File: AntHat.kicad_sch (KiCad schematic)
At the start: 61 parts, among them J1 Raspberry_Pi_2_3, J10 0353180420, J11 0353180420, J2 0455580003, J3 PSU Comm, J4 61900411021, J5 61900411021, J6 61900411021, J7 61900411021, J8 0353180420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

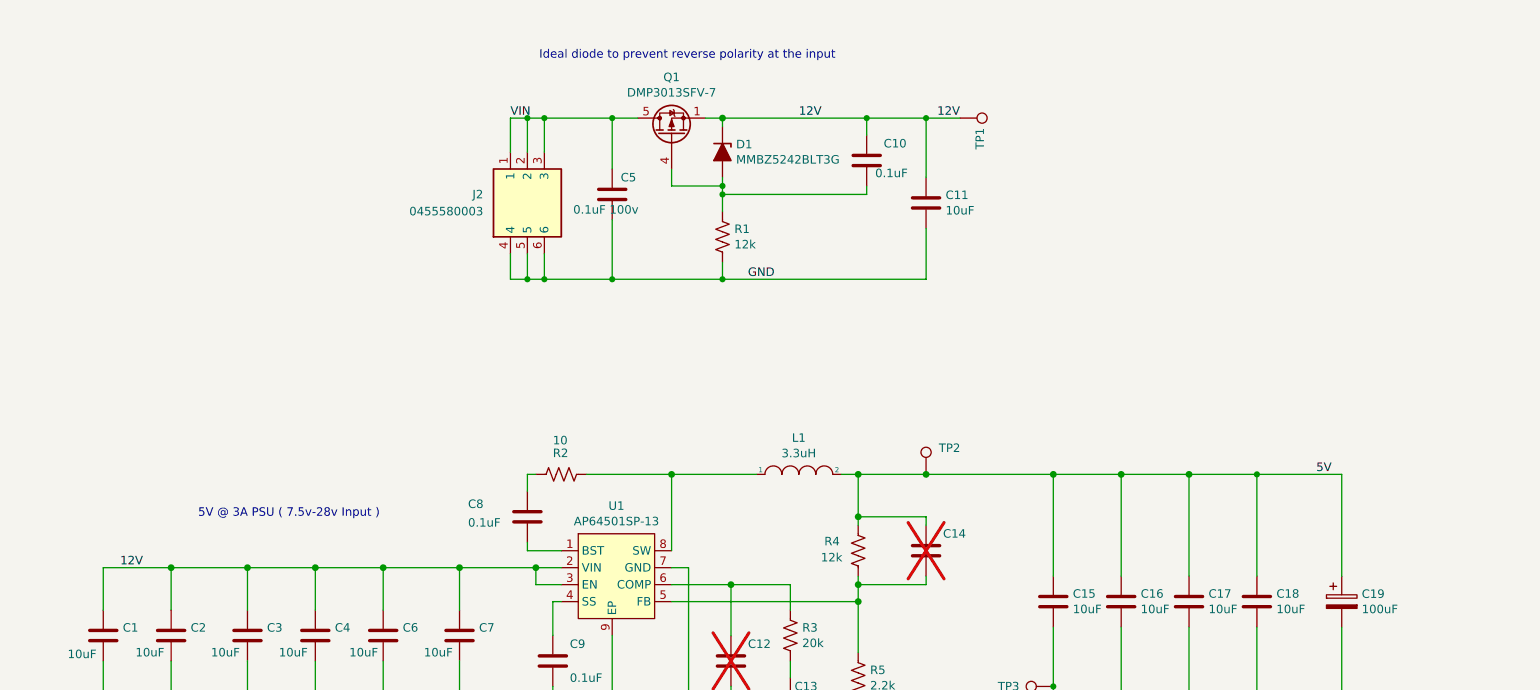
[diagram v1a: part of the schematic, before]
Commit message: started to add TPS259241
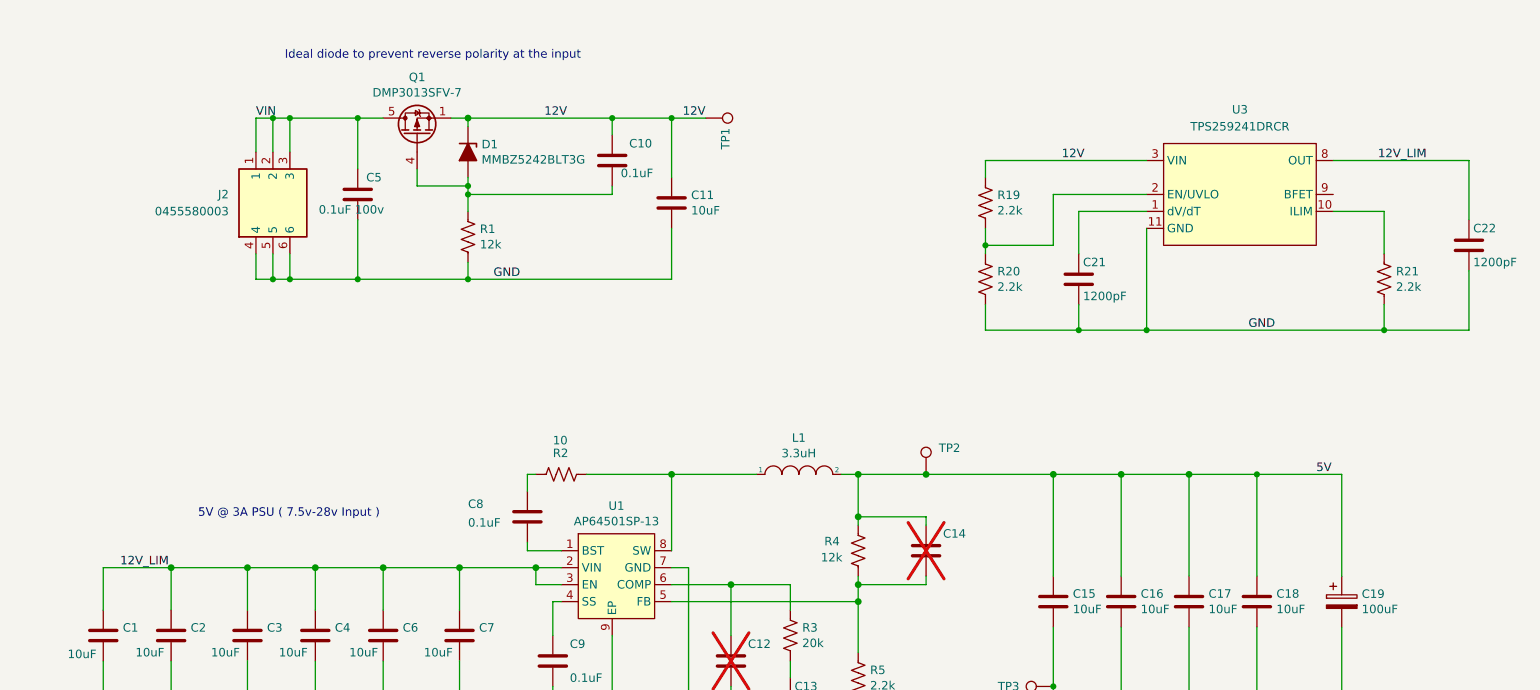
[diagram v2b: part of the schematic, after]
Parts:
- added C21, C22: 1200pF, Capacitor_SMD:C_0402_1005Metric, symbol Device:C
- added R19, R20, R21: 2.2k, Resistor_SMD:R_0402_1005Metric, symbol Device:R_US
- added U3: TPS259241DRCR, AntHat:VSON-10_L3.0-W3.0-P0.50-TL-EP, symbol AntHat:TPS259241DRCR
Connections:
- net 12V: now also R19.1, U3.3 (VIN), U3.4 (VIN), U3.5 (VIN); no longer C1.1, C2.1, C3.1, C4.1, C6.1, C7.1, U1.2 (VIN), U1.3 (EN)
- net GND: now also C21.2, C22.2, R20.2, R21.2, U3.11 (GND)
- new net: R19.2, R20.1, U3.2 (EN/UVLO)
- new net: C21.1, U3.1 (dV/dT)
- new net: R21.1, U3.10 (ILIM)
- new net 12V_LIM: C1.1, C2.1, C22.1, C3.1, C4.1, C6.1, C7.1, U1.2 (VIN), U1.3 (EN), U3.6 (OUT), U3.7 (OUT), U3.8 (OUT)
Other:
- moved on the sheet: C10, C11, C5, D1, J2, Q1, R1, TP1

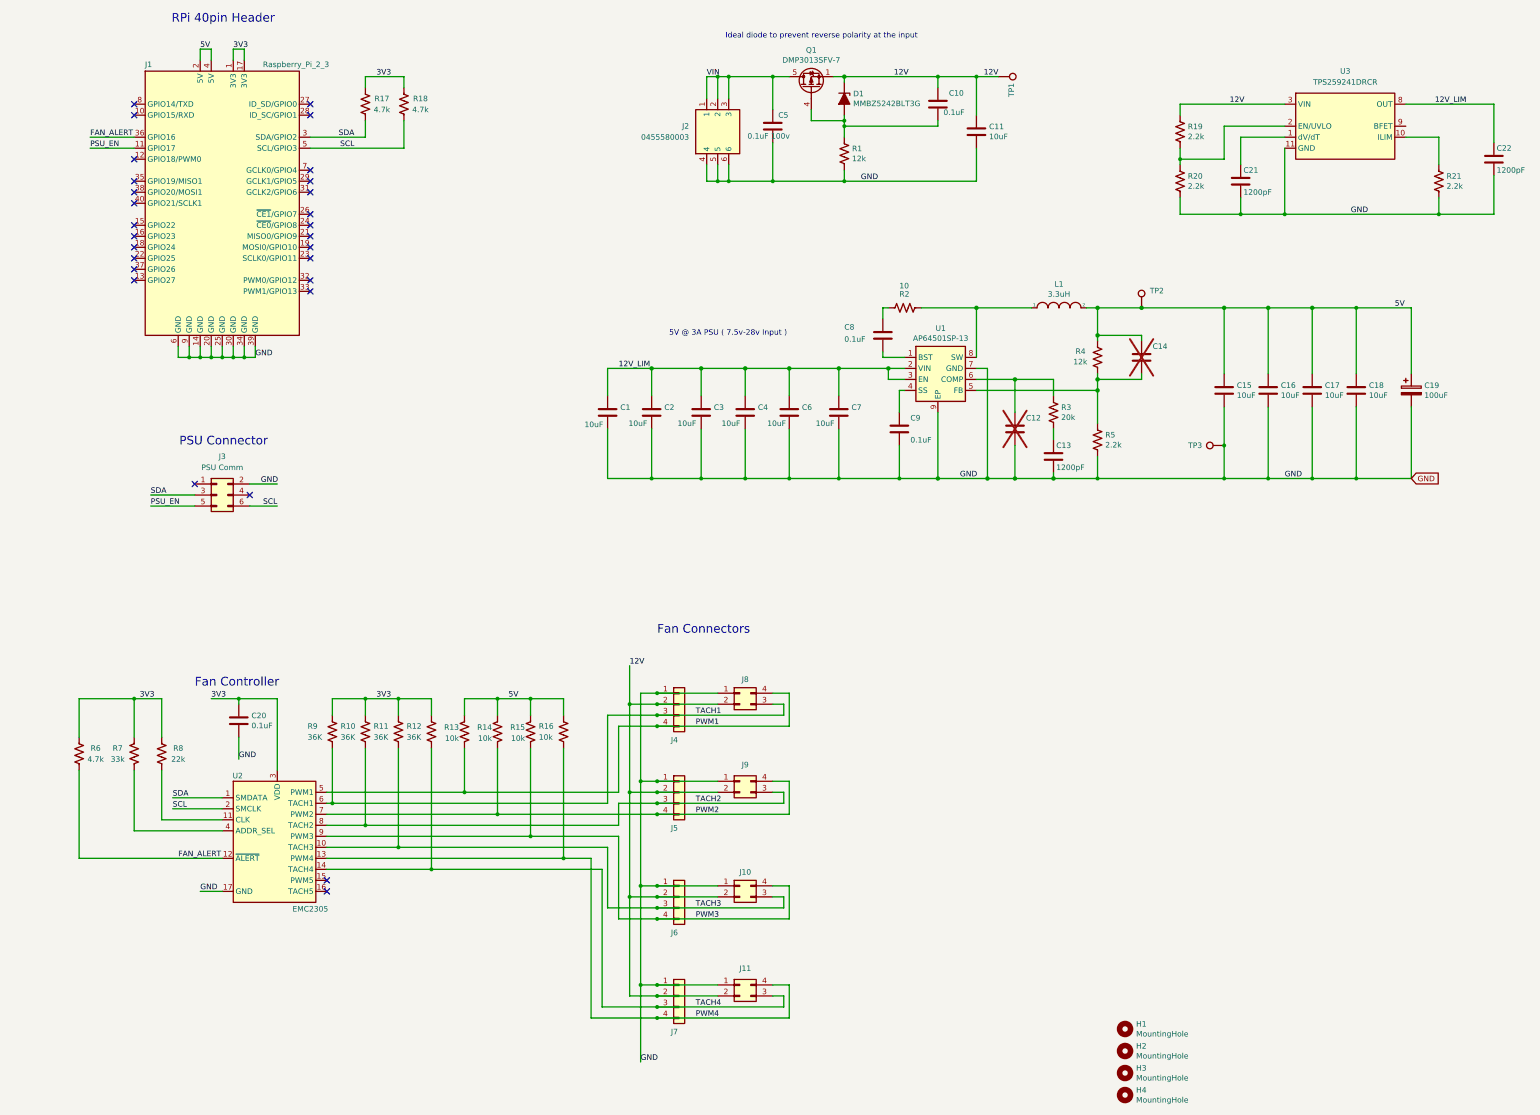
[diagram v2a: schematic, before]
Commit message: combined the fan connector styles. added some LCSC part numbers. switched PSU I2C over to GPIO for bit banging.
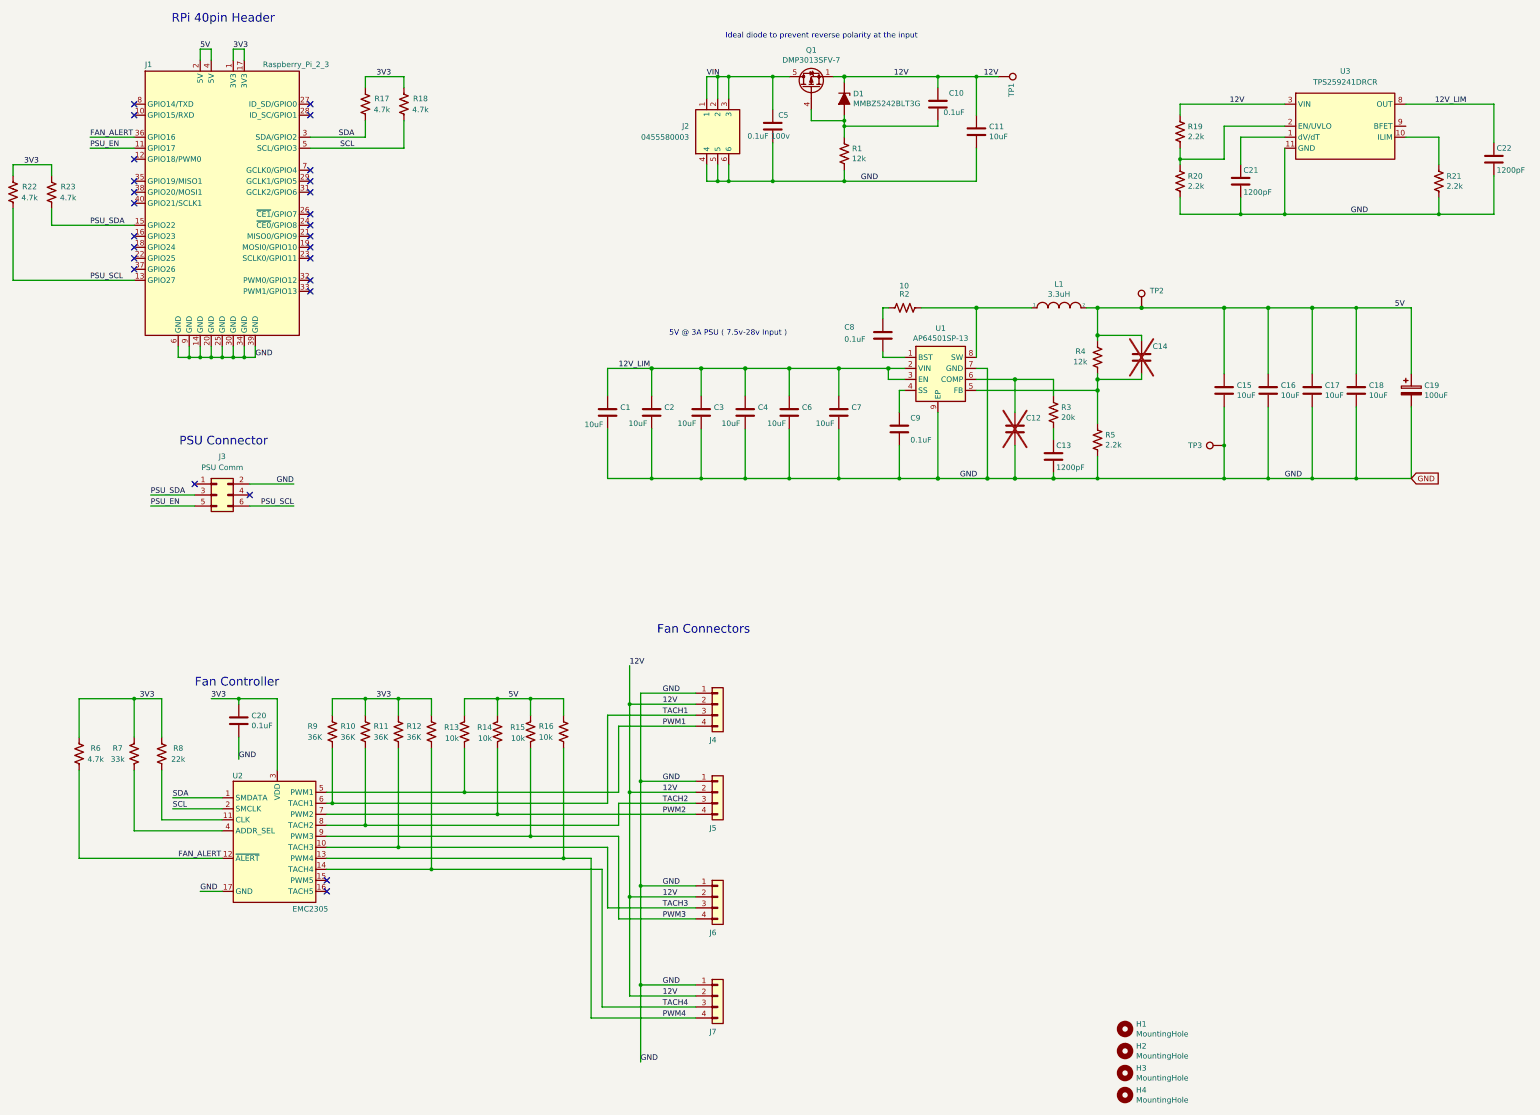
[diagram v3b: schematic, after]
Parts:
- removed J10, J11, J8, J9: 0353180420, AntHat:MOLEX_353180420, symbol Connector_Generic:Conn_02x02_Counter_Clockwise
- added R22, R23: 4.7k, Resistor_SMD:R_0402_1005Metric, symbol Device:R_US
- D1: LCSC (none) -> C12773; PARTNO MMBZ5242BLT3G -> LBZX84C12LT1G
- H1, H2, H3, H4: now left out of the parts list
- J1: LCSC (none) -> C2977589; LCSC Part C2977589 -> (none)
- J2: LCSC (none) -> C19188571; LCSC Part C19188571 -> (none)
- J3: LCSC (none) -> C2845614; LCSC Part C2845614 -> (none)
- J4, J5: footprint AntHat:CONN_61900411021_WRE -> AntHat:MOLEX_1x4_2x2_combo; LCSC (none) -> C2982043
- J6, J7: value 61900411021 -> 0353180420; footprint AntHat:CONN_61900411021_WRE -> AntHat:MOLEX_1x4_2x2_combo; DK 732-2701-ND -> WM13195-ND; LCSC (none) -> C54909; PARTNO 61900411021 -> 0353180420
- L1: LCSC (none) -> C189931; LCSC Part C189931 -> (none)
- Q1: LCSC (none) -> C264098; LCSC Part C264098 -> (none)
- U1: LCSC (none) -> C2071517
- U3: LCSC (none) -> C165131; LCSC Part C165131 -> (none)
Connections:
- net 3V3: now also R22.2, R23.2
- net SCL: no longer J3.6 (Pin_6)
- net SDA: no longer J3.3 (Pin_3)
- net PSU_SCL: now reaches J1.13 (GPIO27)
- net PSU_SCL: now also J3.6 (Pin_6), R22.1
- net PSU_SDA: now reaches J1.15 (GPIO22)
- net PSU_SDA: now also J3.3 (Pin_3), R23.1
- no-connect marks 28 -> 26
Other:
- moved on the sheet: J4, J5, J6, J7

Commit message: fixed the footprint & paste on the TPS259241 footprint. Generated and checked gerbers. Generated BOM. Generated iBOM
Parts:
- U3: DK (none) -> 296-44843-1-ND; PARTNO (none) -> TPS259241DRCR
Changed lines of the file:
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@@
 			)
 		)
-		(property "Datasheet" ""
+		(property "Datasheet" "https://www.ti.com/lit/ds/symlink/tps25924.pdf"
 			(at 330.2 58.42 0)
 			(effects
@@
 			(at 330.2 50.8 0)
 			(effects
+				(font
+					(size 1.27 1.27)
+				)
+				(hide yes)
+			)
+		)
+		(property "DK" "296-44843-1-ND"
+			(at 330.2 50.8 0)
+			(effects
+				(font
+					(size 1.27 1.27)
+				)
+				(hide yes)
+			)
+		)
+		(property "PARTNO" "TPS259241DRCR"
+			(at 330.2 50.8 0)
+			(effects

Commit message: added JLCPCB Parts to BOM. changed one CAP to bigger size, cleaned up layout. regenerated gerbers, BOM and CPOS
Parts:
- C1, C11, C15, C16, C17, C18, C2, C3, C4, C6, C7: LCSC (none) -> C15850; Voltage (none) -> 25V
- C10, C20, C8, C9: LCSC (none) -> C52923; Voltage (none) -> 25V
- C13, C21, C22: LCSC (none) -> C16529; Voltage (none) -> 25V
- C19: LCSC (none) -> C7222; Voltage (none) -> 10V
- C5: value 0.1uF 100v -> 0.1uF; footprint Capacitor_SMD:C_0402_1005Metric -> Capacitor_SMD:C_0805_2012Metric; DK 490-10458-1-ND -> (none); LCSC (none) -> C28233; PARTNO GRM155R62A104KE14D -> (none); Voltage (none) -> 100V
- R1, R4: LCSC (none) -> C25752
- R10, R11, R12, R9: LCSC (none) -> C137999
- R13, R14, R15, R16: LCSC (none) -> C60489
- R17, R18, R22, R23, R6: LCSC (none) -> C25900
- R19, R20, R21, R5: LCSC (none) -> C25879
- R2: LCSC (none) -> C25077
- R3: LCSC (none) -> C25765
- R7: LCSC (none) -> C25779
- R8: LCSC (none) -> C25768
- TP1, TP2, TP3: now left out of the parts list
- U2: LCSC (none) -> C621415

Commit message: updated some OOS LCSC parts. regenerated BOM. added iBOM
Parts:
- C21: LCSC C16529 -> C107021
- J2: LCSC C19188571 -> C492365
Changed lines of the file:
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@@
 			)
 		)
-		(property "LCSC" "C16529"
+		(property "LCSC" "C107021"
 			(at 306.07 63.5 0)
 			(effects
@@
 			)
 		)
-		(property "LCSC" "C19188571"
+		(property "LCSC" "C492365"
 			(at 185.42 52.07 0)
 			(effects

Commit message: switched to 6 layers. moved power vias into pads
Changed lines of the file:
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@@
 (kicad_sch
-	(version 20231120)
+	(version 20250114)
 	(generator "eeschema")
-	(generator_version "8.0")
+	(generator_version "9.0")
 	(paper "A3")
 	(title_block
 		(title "AntHat")
-		(date "2024-04-20")
-		(rev "2")
+		(date "2025-09-21")
+		(rev "3")
+	)
+	(text "RPi 40pin Header"
+		(exclude_from_sim no)
+		(at 59.436 27.178 0)
+		(effects
+			(font
+				(size 2 2)
+			)
+			(justify left bottom)
+		)
+	)
+	(text "Ideal diode to prevent reverse polarity at the input"
+		(exclude_from_sim no)
+		(at 187.198 30.734 0)
+		(effects
+			(font
+				(size 1.27 1.27)
+			)
+			(justify left bottom)
+		)
+	)
+	(text "5V @ 3A PSU ( 7.5v-28v Input )"
+		(exclude_from_sim no)
+		(at 201.422 99.314 0)
+		(effects
+			(font
+				(size 1.27 1.27)
+			)
+			(justify right bottom)
+		)
+	)
+	(text "Fan Connectors"
+		(exclude_from_sim no)
+		(at 171.45 168.148 0)
+		(effects
+			(font
+				(size 2 2)
+			)
+			(justify left bottom)
+		)
+	)
+	(text "PSU Connector"
+		(exclude_from_sim no)
+		(at 61.214 124.714 0)
+		(effects
+			(font
+				(size 2 2)
+			)
+			(justify left bottom)
+		)
+	)
+	(text "Fan Controller"
+		(exclude_from_sim no)
+		(at 64.77 180.34 0)
+		(effects
+			(font
+				(size 2.0066 2.0066)
+			)
+			(justify left bottom)
+		)
 	)
 	(junction
@@
 		)
 	)
-	(text "RPi 40pin Header"
-		(exclude_from_sim no)
-		(at 59.436 27.178 0)
-		(effects
-			(font
-				(size 2 2)
-			)
-			(justify left bottom)
-		)
-	)
-	(text "Ideal diode to prevent reverse polarity at the input"
-		(exclude_from_sim no)
-		(at 187.198 30.734 0)
-		(effects
-			(font
-				(size 1.27 1.27)
-			)
-			(justify left bottom)
-		)
-	)
-	(text "5V @ 3A PSU ( 7.5v-28v Input )"
-		(exclude_from_sim no)
-		(at 201.422 99.314 0)
-		(effects
-			(font
-				(size 1.27 1.27)
-			)
-			(justify right bottom)
-		)
-	)
-	(text "Fan Connectors"
-		(exclude_from_sim no)
-		(at 171.45 168.148 0)
-		(effects
-			(font
-				(size 2 2)
-			)
-			(justify left bottom)
-		)
-	)
-	(text "PSU Connector"
-		(exclude_from_sim no)
-		(at 61.214 124.714 0)
-		(effects
-			(font
-				(size 2 2)
-			)
-			(justify left bottom)
-		)
-	)
-	(text "Fan Controller"
-		(exclude_from_sim no)
-		(at 64.77 180.34 0)
-		(effects
-			(font
-				(size 2.0066 2.0066)
-			)
-			(justify left bottom)
-		)
-	)
 	(label "SCL"
 		(at 101.6 55.88 180)
-		(fields_autoplaced yes)
 		(effects
 			(font
@@
 	(label "12V_LIM"
 		(at 358.14 45.72 180)
-		(fields_autoplaced yes)
 		(effects
 			(font
@@
 	(label "SDA"
 		(at 101.6 53.34 180)
-		(fields_autoplaced yes)
 		(effects
 			(font
@@
 	(label "12V"
 		(at 172.72 228.6 0)
-		(fields_autoplaced yes)
 		(effects
 			(font
@@
 	(label "SDA"
 		(at 59.69 205.74 0)
-		(fields_autoplaced yes)
 		(effects
 			(font
@@
 	(label "3V3"
 		(at 52.07 182.88 0)
-		(fields_autoplaced yes)
 		(effects
 			(font
@@
 	(label "PWM3"
 		(at 172.72 233.68 0)
-		(fields_autoplaced yes)
 		(effects
 			(font
@@
 	(label "TACH1"
 		(at 172.72 186.69 0)
-		(fields_autoplaced yes)
 		(effects
 			(font
@@
 	(label "GND"
 		(at 167.64 266.7 0)
-		(fields_autoplaced yes)
 		(effects
 			(font
@@
 	(label "FAN_ALERT"
 		(at 40.64 53.34 0)
-		(fields_autoplaced yes)
 		(effects
 			(font
@@
 	(label "FAN_ALERT"
 		(at 60.96 219.71 0)
-		(fields_autoplaced yes)
 		(effects
 			(font
@@
 	(label "TACH3"
 		(at 172.72 231.14 0)
-		(fields_autoplaced yes)
 		(effects
 			(font
@@
 	(label "3V3"
 		(at 106.68 182.88 0)
-		(fields_autoplaced yes)
 		(effects
 			(font
@@
 	(label "12V"
 		(at 226.06 39.37 0)
-		(fields_autoplaced yes)
 		(effects
 			(font
@@
 	(label "GND"
 		(at 78.74 104.14 0)
-		(fields_autoplaced yes)
 		(effects
 			(font
@@
 	(label "PSU_SCL"
 		(at 87.63 138.43 180)
-		(fields_autoplaced yes)
 		(effects
 			(font
@@
 	(label "GND"
 		(at 172.72 248.92 0)
-		(fields_autoplaced yes)
 		(effects
 			(font
@@
 	(label "12V"
 		(at 303.53 45.72 0)
-		(fields_autoplaced yes)
 		(effects
 			(font
@@
 	(label "VIN"
 		(at 182.88 39.37 0)
-		(fields_autoplaced yes)
 		(effects
 			(font
@@
 	(label "3V3"
 		(at 25.4 59.69 0)
-		(fields_autoplaced yes)
 		(effects
 			(font
@@
 	(label "GND"
 		(at 331.47 71.12 0)
-		(fields_autoplaced yes)
 		(effects
 			(font
@@
 	(label "3V3"
 		(at 68.58 182.88 0)
-		(fields_autoplaced yes)
 		(effects
 			(font
@@
 	(label "GND"
 		(at 66.04 227.33 0)
-		(fields_autoplaced yes)
 		(effects
 			(font
@@
 	(label "TACH4"
 		(at 172.72 254 0)
-		(fields_autoplaced yes)
 		(effects
 			(font
@@
 	(label "GND"
 		(at 218.44 63.5 0)
-		(fields_autoplaced yes)
 		(effects
 			(font
@@
 	(label "12V"
 		(at 165.1 175.26 0)
-		(fields_autoplaced yes)
 		(effects
 			(font
@@
 	(label "GND"
 		(at 74.93 196.85 0)
-		(fields_autoplaced yes)
 		(effects
 			(font
@@
 	(label "5V"
 		(at 137.16 182.88 0)
-		(fields_autoplaced yes)
 		(effects
 			(font
@@
 	(label "3V3"
 		(at 73.66 33.02 0)
-		(fields_autoplaced yes)
 		(effects
 			(font
@@
 	(label "PSU_SDA"
 		(at 54.61 135.89 0)
-		(fields_autoplaced yes)
 		(effects
 			(font
@@
 	(label "12V"
 		(at 250.19 39.37 180)
-		(fields_autoplaced yes)
 		(effects
 			(font
@@
 	(label "TACH2"
 		(at 172.72 207.01 0)
-		(fields_autoplaced yes)
 		(effects
 			(font
@@
 	(label "PSU_SDA"
 		(at 40.64 73.66 0)
-		(fields_autoplaced yes)
 		(effects
 			(font
@@
 	(label "PSU_EN"
 		(at 40.64 55.88 0)
-		(fields_autoplaced yes)
 		(effects
 			(font
@@
 	(label "GND"
 		(at 172.72 201.93 0)
-		(fields_autoplaced yes)
 		(effects
 			(font
@@
 	(label "12V"
 		(at 172.72 204.47 0)
-		(fields_autoplaced yes)
 		(effects
 			(font
@@
 	(label "SCL"
 		(at 59.69 208.28 0)
-		(fields_autoplaced yes)
 		(effects
 			(font
@@
 	(label "PWM1"
 		(at 172.72 189.23 0)
-		(fields_autoplaced yes)
 		(effects
 			(font
@@
 	(label "PWM4"
 		(at 172.72 256.54 0)
-		(fields_autoplaced yes)
 		(effects
 			(font
@@
 	(label "PSU_EN"
 		(at 54.61 138.43 0)
-		(fields_autoplaced yes)
 		(effects
 			(font
@@
 	(label "12V"
 		(at 172.72 251.46 0)
-		(fields_autoplaced yes)
 		(effects
 			(font
@@
 	(label "PSU_SCL"
 		(at 40.64 86.36 0)
-		(fields_autoplaced yes)
 		(effects
 			(font
@@
 	(label "5V"
 		(at 341.63 92.71 0)
-		(fields_autoplaced yes)
 		(effects
 			(font
@@
 	(label "GND"
 		(at 172.72 181.61 0)
-		(fields_autoplaced yes)
 		(effects
 			(font
@@
 	(label "GND"
 		(at 87.63 133.35 180)
-		(fields_autoplaced yes)
 		(effects
 			(font
@@
 	(label "GND"
 		(at 241.3 132.08 0)
-		(fields_autoplaced yes)
 		(effects
 			(font
@@
 	(label "5V"
 		(at 66.04 33.02 0)
-		(fields_autoplaced yes)
 		(effects
 			(font
@@
 	(label "GND"
 		(at 172.72 226.06 0)
-		(fields_autoplaced yes)
 		(effects
 			(font
@@
 	(label "GND"
 		(at 316.23 132.08 0)
-		(fields_autoplaced yes)
 		(effects
 			(font
@@
 	(label "3V3"
 		(at 106.68 39.37 0)
-		(fields_autoplaced yes)
 		(effects
 			(font
@@
 	(label "12V_LIM"
 		(at 162.56 106.68 0)
-		(fields_autoplaced yes)
 		(effects
 			(font
@@
 	(label "12V"
 		(at 172.72 184.15 0)
-		(fields_autoplaced yes)
 		(effects
 			(font
@@
 	(label "PWM2"
 		(at 172.72 209.55 0)
-		(fields_autoplaced yes)
 		(effects
 			(font
@@
 		)
 	)
+	(embedded_fonts no)
 )
